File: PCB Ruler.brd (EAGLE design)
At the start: 76.2 x 12.7 mm, 1 part

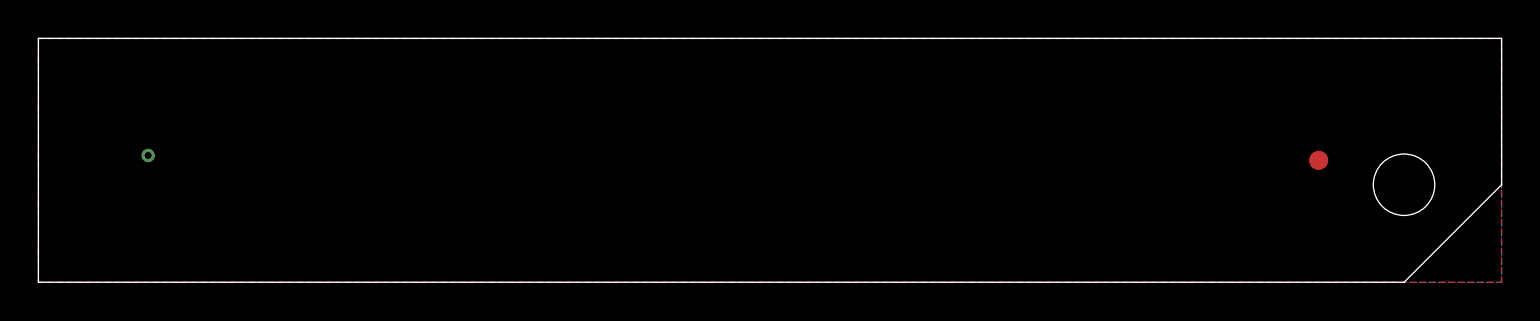
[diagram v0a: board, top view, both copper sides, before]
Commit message: Modified Silkscreen and placement of hole.
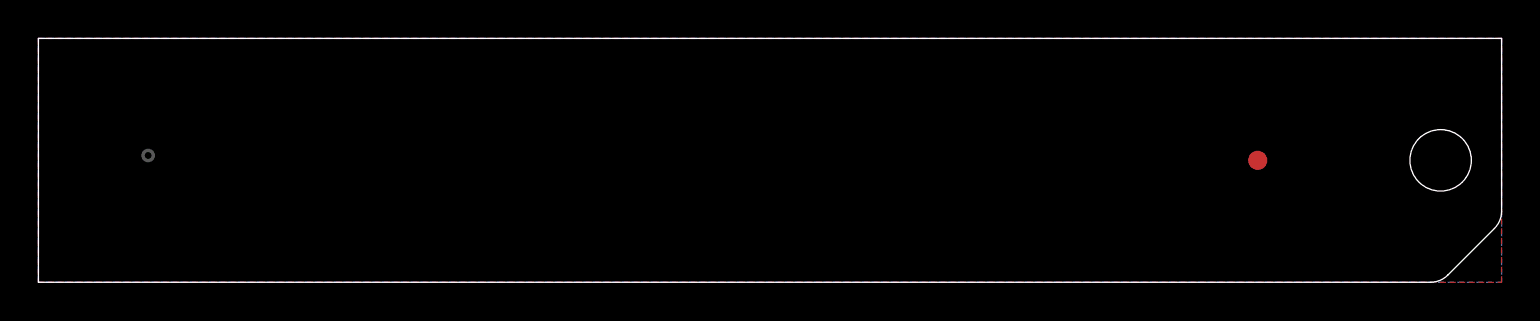
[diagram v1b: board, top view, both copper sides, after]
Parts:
- moved U$2 3.17 mm to (63.5, 6.35)
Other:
- outline, holes or cut-outs redrawn
- board text added: "7"
